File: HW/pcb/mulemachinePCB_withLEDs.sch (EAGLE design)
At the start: 33 parts, among them IC1 LD117AV50, IC2 MEGA8-P, J1 DCJ0202, Q1 16Mhz

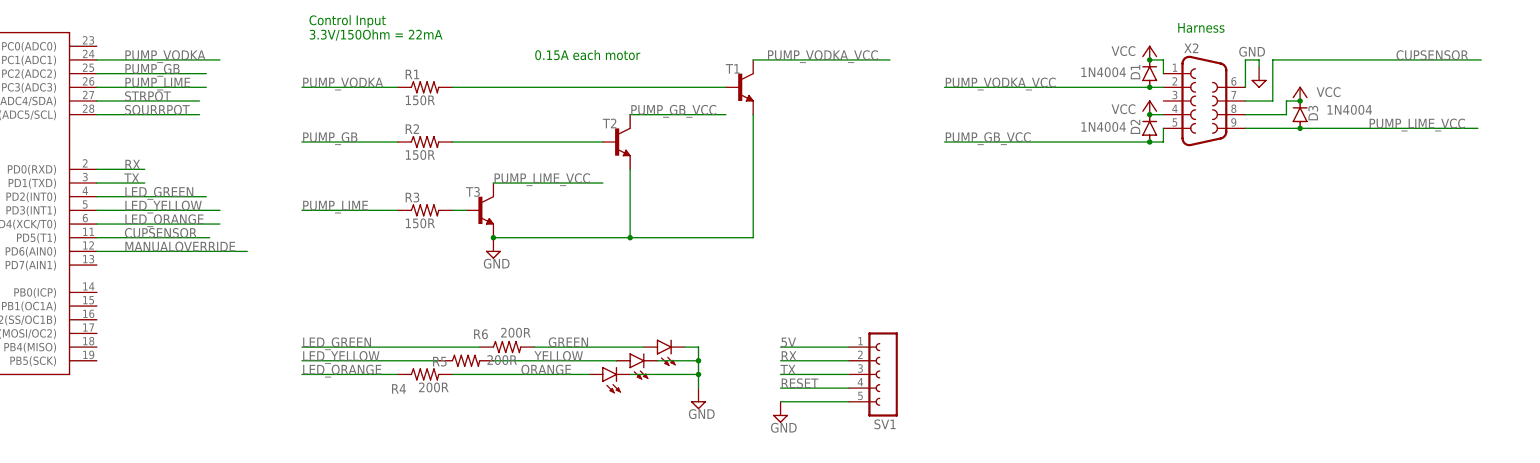
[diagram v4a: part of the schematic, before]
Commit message: repinned LED and pump pins on MCU to use PWM digital pins. need to check and then reroute PCB and redo GND planes
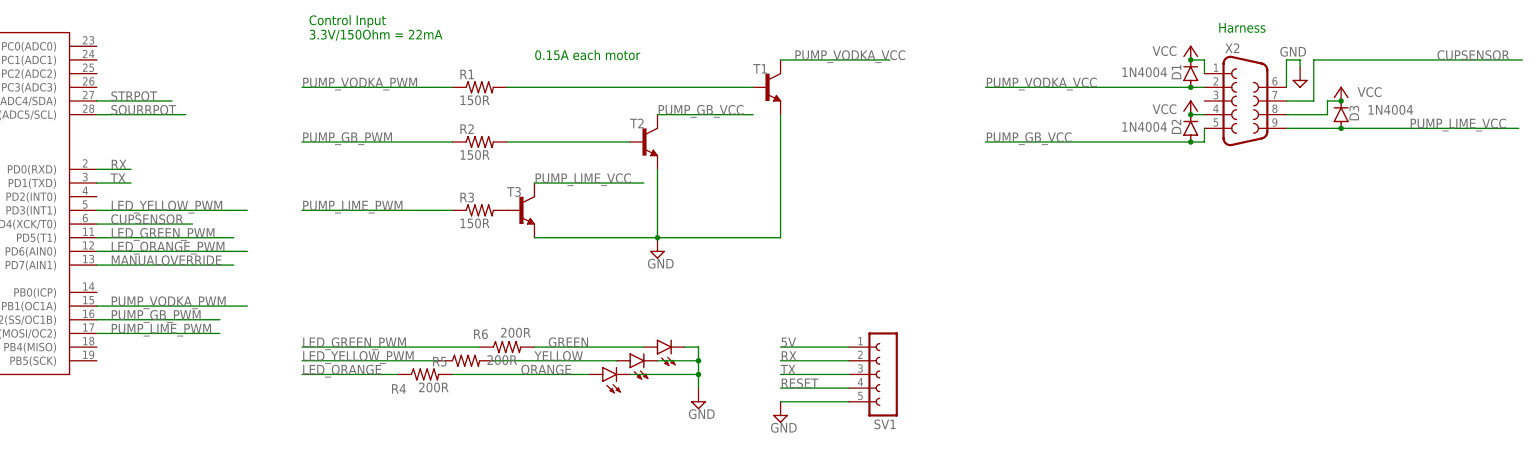
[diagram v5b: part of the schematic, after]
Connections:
- net LED_YELLOW renamed LED_YELLOW_PWM
- removed net LED_GREEN: IC2.PD2(INT0), R6.1
- removed net PUMP_GB: IC2.PC2(ADC2), R2.1
- removed net PUMP_LIME: IC2.PC3(ADC3), R3.1
- removed net PUMP_VODKA: IC2.PC1(ADC1), R1.1
- new net LED_GREEN_PWM: IC2.PD5(T1), R6.1
- new net LED_ORANGE_PWM: IC2.PD6(AIN0)
- new net PUMP_GB_PWM: IC2.PB2(SS/OC1B), R2.1
- new net PUMP_LIME_PWM: IC2.PB3(MOSI/OC2), R3.1
- new net PUMP_VODKA_PWM: IC2.PB1(OC1A), R1.1
- net CUPSENSOR: now also IC2.PD4(XCK/T0); no longer IC2.PD5(T1)
- net LED_ORANGE: no longer IC2.PD4(XCK/T0)
- net MANUALOVERRIDE: now also IC2.PD7(AIN1); no longer IC2.PD6(AIN0)
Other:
- moved on the sheet: D1, D2, D3, R1, R2, R3, T1, T2, T3, X2

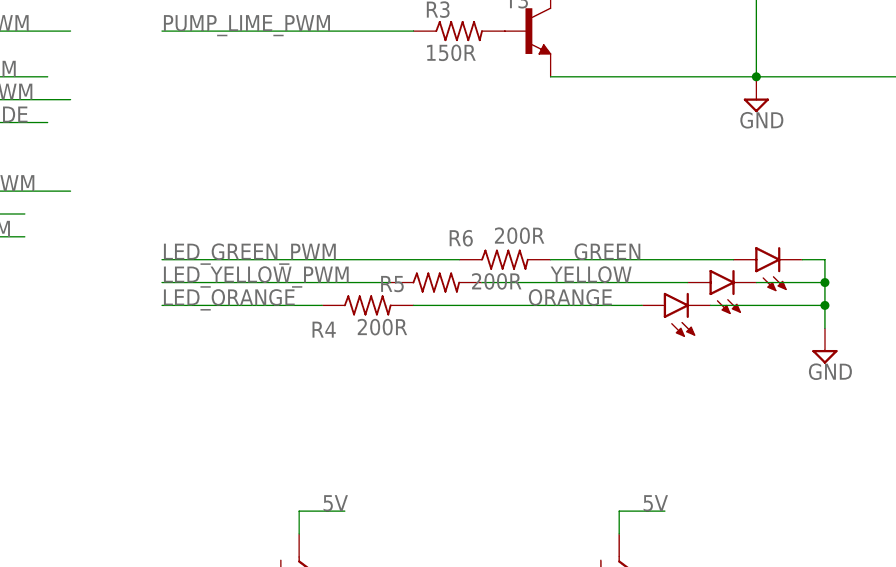
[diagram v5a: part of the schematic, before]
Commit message: fixed issue with mismatch in names for orange LED signal PWM signal name. corrected, regenerated CAM data, reordered PCBs, and remade PNGs
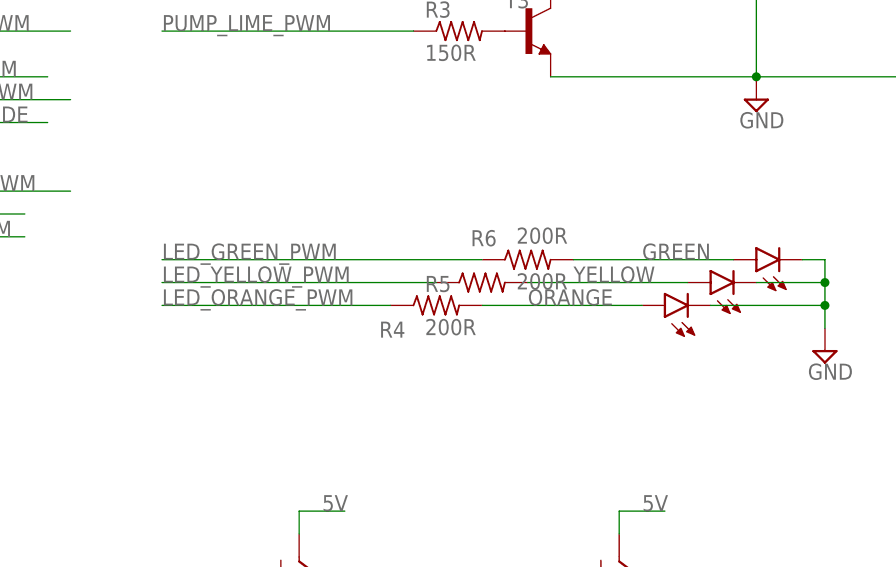
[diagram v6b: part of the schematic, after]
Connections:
- removed net LED_ORANGE: R4.1
- net LED_ORANGE_PWM: now also R4.1
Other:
- moved on the sheet: R4, R5, R6
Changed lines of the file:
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@@
 <attribute name="VALUE" x="140.97" y="77.978" size="1.778" layer="96"/>
 </instance>
-<instance part="R4" gate="G$1" x="134.62" y="50.8" smashed="yes" grouprefs="USER_INTERFACE">
-<attribute name="NAME" x="128.27" y="47.2186" size="1.778" layer="95"/>
-<attribute name="VALUE" x="133.35" y="47.498" size="1.778" layer="96"/>
-</instance>
-<instance part="R5" gate="G$1" x="142.24" y="53.34" smashed="yes" grouprefs="USER_INTERFACE">
-<attribute name="NAME" x="135.89" y="52.2986" size="1.778" layer="95"/>
-<attribute name="VALUE" x="146.05" y="52.578" size="1.778" layer="96"/>
-</instance>
-<instance part="R6" gate="G$1" x="149.86" y="55.88" smashed="yes" grouprefs="USER_INTERFACE">
-<attribute name="NAME" x="143.51" y="57.3786" size="1.778" layer="95"/>
-<attribute name="VALUE" x="148.59" y="57.658" size="1.778" layer="96"/>
+<instance part="R4" gate="G$1" x="142.24" y="50.8" smashed="yes" grouprefs="USER_INTERFACE">
+<attribute name="NAME" x="135.89" y="47.2186" size="1.778" layer="95"/>
+<attribute name="VALUE" x="140.97" y="47.498" size="1.778" layer="96"/>
+</instance>
+<instance part="R5" gate="G$1" x="147.32" y="53.34" smashed="yes" grouprefs="USER_INTERFACE">
+<attribute name="NAME" x="140.97" y="52.2986" size="1.778" layer="95"/>
+<attribute name="VALUE" x="151.13" y="52.578" size="1.778" layer="96"/>
+</instance>
+<instance part="R6" gate="G$1" x="152.4" y="55.88" smashed="yes" grouprefs="USER_INTERFACE">
+<attribute name="NAME" x="146.05" y="57.3786" size="1.778" layer="95"/>
+<attribute name="VALUE" x="151.13" y="57.658" size="1.778" layer="96"/>
 </instance>
 <instance part="IC1" gate="G$1" x="-40.64" y="109.22" smashed="yes" grouprefs="12VTO5V">
@@
 <pinref part="LED1" gate="G$1" pin="A"/>
 <pinref part="R4" gate="G$1" pin="2"/>
-<wire x1="165.1" y1="50.8" x2="139.7" y2="50.8" width="0.1524" layer="91" grouprefs="USER_INTERFACE"/>
+<wire x1="165.1" y1="50.8" x2="147.32" y2="50.8" width="0.1524" layer="91" grouprefs="USER_INTERFACE"/>
 <label x="152.4" y="50.8" size="1.778" layer="95" grouprefs="USER_INTERFACE"/>
 </segment>
@@
 <pinref part="LED2" gate="G$1" pin="A"/>
 <pinref part="R5" gate="G$1" pin="2"/>
-<wire x1="170.18" y1="53.34" x2="147.32" y2="53.34" width="0.1524" layer="91" grouprefs="USER_INTERFACE"/>
-<label x="154.94" y="53.34" size="1.778" layer="95" grouprefs="USER_INTERFACE"/>
+<wire x1="170.18" y1="53.34" x2="152.4" y2="53.34" width="0.1524" layer="91" grouprefs="USER_INTERFACE"/>
+<label x="157.48" y="53.34" size="1.778" layer="95" grouprefs="USER_INTERFACE"/>
 </segment>
 </net>
@@
 <pinref part="R6" gate="G$1" pin="2"/>
 <pinref part="LED3" gate="G$1" pin="A"/>
-<wire x1="154.94" y1="55.88" x2="175.26" y2="55.88" width="0.1524" layer="91" grouprefs="USER_INTERFACE"/>
-<label x="157.48" y="55.88" size="1.778" layer="95" grouprefs="USER_INTERFACE"/>
+<wire x1="157.48" y1="55.88" x2="175.26" y2="55.88" width="0.1524" layer="91" grouprefs="USER_INTERFACE"/>
+<label x="165.1" y="55.88" size="1.778" layer="95" grouprefs="USER_INTERFACE"/>
 </segment>
 </net>
@@
 <segment>
 <pinref part="R6" gate="G$1" pin="1"/>
-<wire x1="111.76" y1="55.88" x2="144.78" y2="55.88" width="0.1524" layer="91" grouprefs="USER_INTERFACE"/>
+<wire x1="111.76" y1="55.88" x2="147.32" y2="55.88" width="0.1524" layer="91" grouprefs="USER_INTERFACE"/>
 <label x="111.76" y="55.88" size="1.778" layer="95" grouprefs="USER_INTERFACE"/>
 </segment>
@@
 <segment>
 <pinref part="R5" gate="G$1" pin="1"/>
-<wire x1="111.76" y1="53.34" x2="137.16" y2="53.34" width="0.1524" layer="91" grouprefs="USER_INTERFACE"/>
+<wire x1="111.76" y1="53.34" x2="142.24" y2="53.34" width="0.1524" layer="91" grouprefs="USER_INTERFACE"/>
 <label x="111.76" y="53.34" size="1.778" layer="95" grouprefs="USER_INTERFACE"/>
 </segment>
@@
 </segment>
 </net>
-<net name="LED_ORANGE" class="0">
-<segment>
-<pinref part="R4" gate="G$1" pin="1"/>
-<wire x1="111.76" y1="50.8" x2="129.54" y2="50.8" width="0.1524" layer="91" grouprefs="USER_INTERFACE"/>
-<label x="111.76" y="50.8" size="1.778" layer="95" grouprefs="USER_INTERFACE"/>
-</segment>
-</net>
 <net name="LED_ORANGE_PWM" class="0">
 <segment>
@@
 <label x="76.2" y="73.66" size="1.778" layer="95" grouprefs="MCU"/>
 </segment>
-</net>
+<segment>
+<pinref part="R4" gate="G$1" pin="1"/>
+<wire x1="111.76" y1="50.8" x2="137.16" y2="50.8" width="0.1524" layer="91" grouprefs="USER_INTERFACE"/>
+<label x="111.76" y="50.8" size="1.778" layer="95" grouprefs="USER_INTERFACE"/>
+</segment>
+</net>
